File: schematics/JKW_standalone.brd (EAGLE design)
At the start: 159.4 x 80.7 mm, 221 parts, among them IC1 4093D, IC2 AT-MEGA-8, IC4 ATMEGA2560-16AU, T1 Mouser: 771-2N7002BK215 , N-C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, T10 Mouser: 771-2N7002BK215 , N-C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, T11 Mouser: 771-2N7002BK215 , N-C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, T12 Mouser: 771-2N7002BK215 , N-C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, T2 Mouser: 771-2N7002BK215 , N-C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, T3 Mouser: 771-2N7002BK215 , N-C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, T4 T-IRLMS6702, T5 Mouser: 771-2N7002BK215 , N-C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, T6 Mouser: 771-2N7002BK215 , N-C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, T7 Mouser: 771-2N7002BK215 , N-C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, T8 Mouser: 771-2N7002BK215 , N-C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, T9 Mouser: 771-2N7002BK215 , N-C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

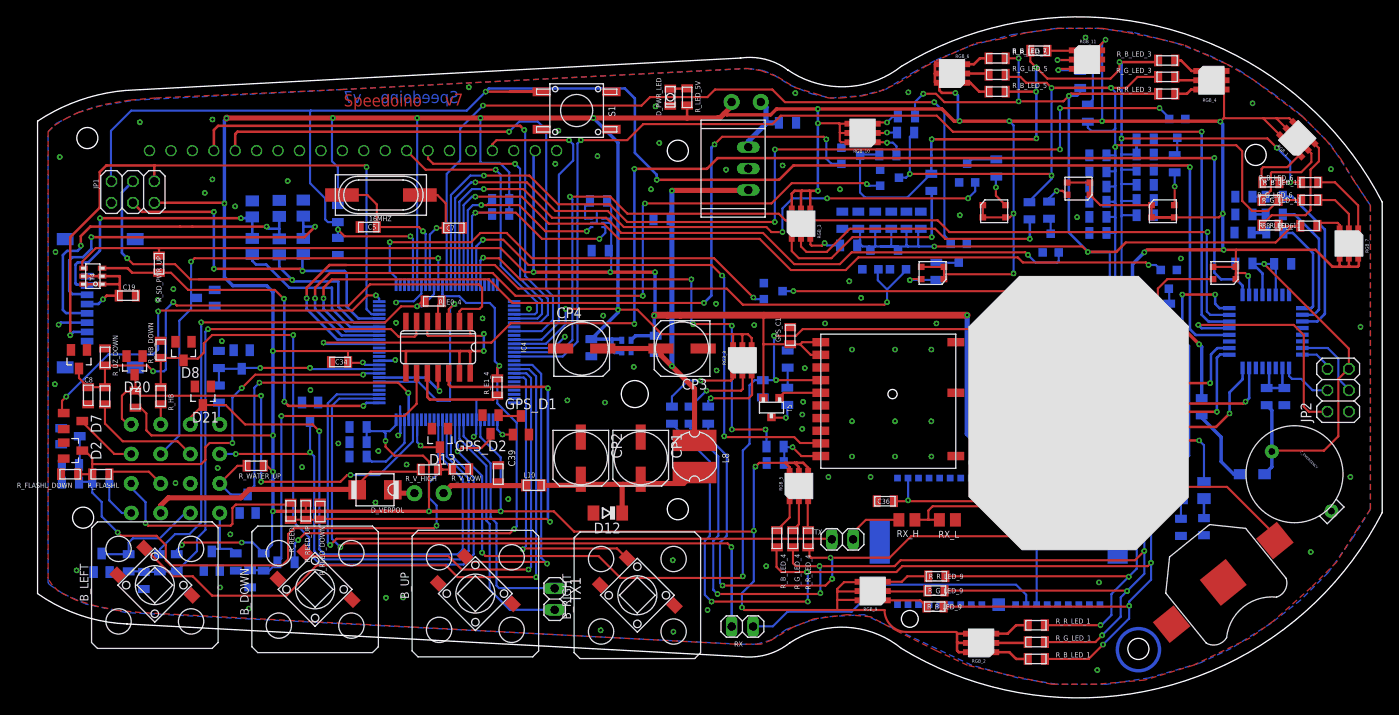
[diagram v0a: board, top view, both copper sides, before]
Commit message: Added Voltage measure wire, buffered
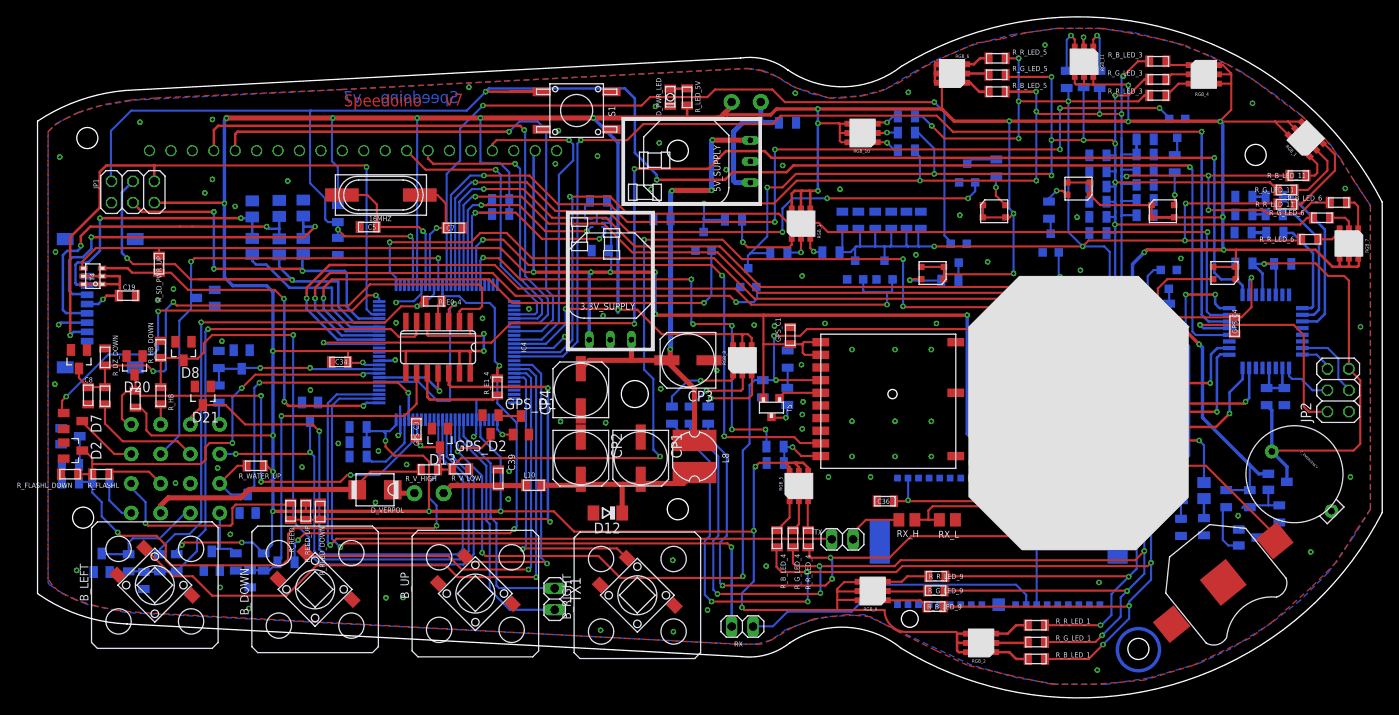
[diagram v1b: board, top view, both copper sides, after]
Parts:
- removed C4: 4.7µF, RCLDT:0805
- removed C6: 10uF, RCLDT:0805
- removed D11: Mouser 726-BAT60AE6327, diode:SOD323-W
- removed DC3.3: LXDC2HL33A-055, Kolja:LXDC2HL33A-055
- removed PWR_R78: R-7805-1.0, Kolja:SIP3
- removed R_L3: 0R, RCLDT:0805
- added 3.3V_SUPPLY: OKI78SR3.31.5WHC, Kolja:OKI-78SR
- added 5V_SUPPLY: OKI78SR51.5W36HC, Kolja:OKI-78SR
- added GPS_C3, GPS_C4: 100nF, RCLDT:0805
- added R_L4, R_L5: 2,1K, RCLDT:0805
- added R_L6: 21k, RCLDT:0805
- added T13: (no value), transistor:SOT23-BEC
- added U$14: 2N7002K, Kolja:SOT23
- IC2: value AT-MEGA-8 -> AT-MEGA-8L
- moved T11 30.4 mm to (117.6, 43.2)
- moved R_G_LED_2 30.1 mm to (87.9, 48.2), turned to 0 degrees
- moved R_B_LED_2 23.9 mm to (82.5, 52.0), turned to 0 degrees
- moved T2 20.5 mm to (84.2, 45.2), turned to 180 degrees
- moved T1 20.2 mm to (79.0, 49.5), turned to 180 degrees
- moved R_B_LED_7 7.96 mm to (125.9, 68.7), flipped to the bottom, turned to 270 degrees
- moved CP4 4.90 mm to (64.4, 31.9), turned to 90 degrees
- moved R_B_LED_6 4.16 mm to (154.2, 54.1)
- moved R_G_LED_7 4.13 mm to (124.0, 68.8)
- moved RGB_11 3.41 mm to (125.7, 69.3), turned to 90 degrees
- moved R_B_LED_11 3.30 mm to (149.4, 57.3), turned to 180 degrees
- moved R_R_LED_11 3.14 mm to (148.0, 53.9), turned to 180 degrees
- moved R_G_LED_6 2.52 mm to (152.2, 52.3)
- moved R_B_LED_8 2.26 mm to (103.0, 60.3), turned to 180 degrees
- moved R_R_LED_2 2.25 mm to (94.0, 48.2)
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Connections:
- removed net N$70: D11.A, R_L3.1
- new net N$86: R_L6.2, U$14.1
- new net N$87: R_L4.1, U$14.3
- new net N$88: R_L4.2, R_L5.2, T13.B
- net +3V3_EXT: now also 3.3V_SUPPLY.OUT; no longer C6.2, DC3.3.V_OUT
- net A2: now also GPS_C3.2, GPS_C4.2, IC2.2
- net BAT+: now also 3.3V_SUPPLY.IN, 5V_SUPPLY.IN; no longer PWR_R78.IN
- net GND: now also 3.3V_SUPPLY.GND, 5V_SUPPLY.GND, GPS_C3.1, GPS_C4.1, U$14.2; no longer C4.1, C6.1, DC3.3.GND, PWR_R78.GND
- net N$19: now also 5V_SUPPLY.OUT; no longer PWR_R78.OUT
- net VDD: now also R_L5.1, R_L6.1, T13.E; no longer C4.2, DC3.3.EN, DC3.3.V_IN, IC2.2, R_L3.2
- net V_AT8_BUFFERED: now also T13.C; no longer D11.C
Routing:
- net A2: track 12.0 -> 150.4 mm, vias 1 -> 6
- net GREEN_INSTR: track 277.0 -> 319.4 mm, vias 11 -> 16
- net BLUE_INSTR: track 292.3 -> 323.5 mm, vias 14 -> 17
- net D9: track 94.3 -> 63.5 mm, vias 4 -> 2
- net D13: track 53.4 -> 84.0 mm
- net N$71: track 37.5 -> 6.97 mm, vias 2 -> 0
- net N$55: track 32.6 -> 3.52 mm
- net D8: track 92.5 -> 67.5 mm, vias 4 -> 2
- net RED_INSTR: track 288.5 -> 305.5 mm, vias 12 -> 15
- net N$56: track 25.3 -> 9.86 mm
- net V_AT8_BUFFERED: track 53.3 -> 62.8 mm
- net N$70: track 9.31 -> 0.00 mm
- net BAT+: track 50.5 -> 59.7 mm, vias 2 -> 4
- net VDD: track 783.9 -> 792.3 mm, vias 41 -> 38
- net N$19: track 8.06 -> 16.2 mm
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
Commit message: Added PWR Pads, Added second 100nF cap to reduce ripple at the GPS, added resistors to save the z-diodes from over current
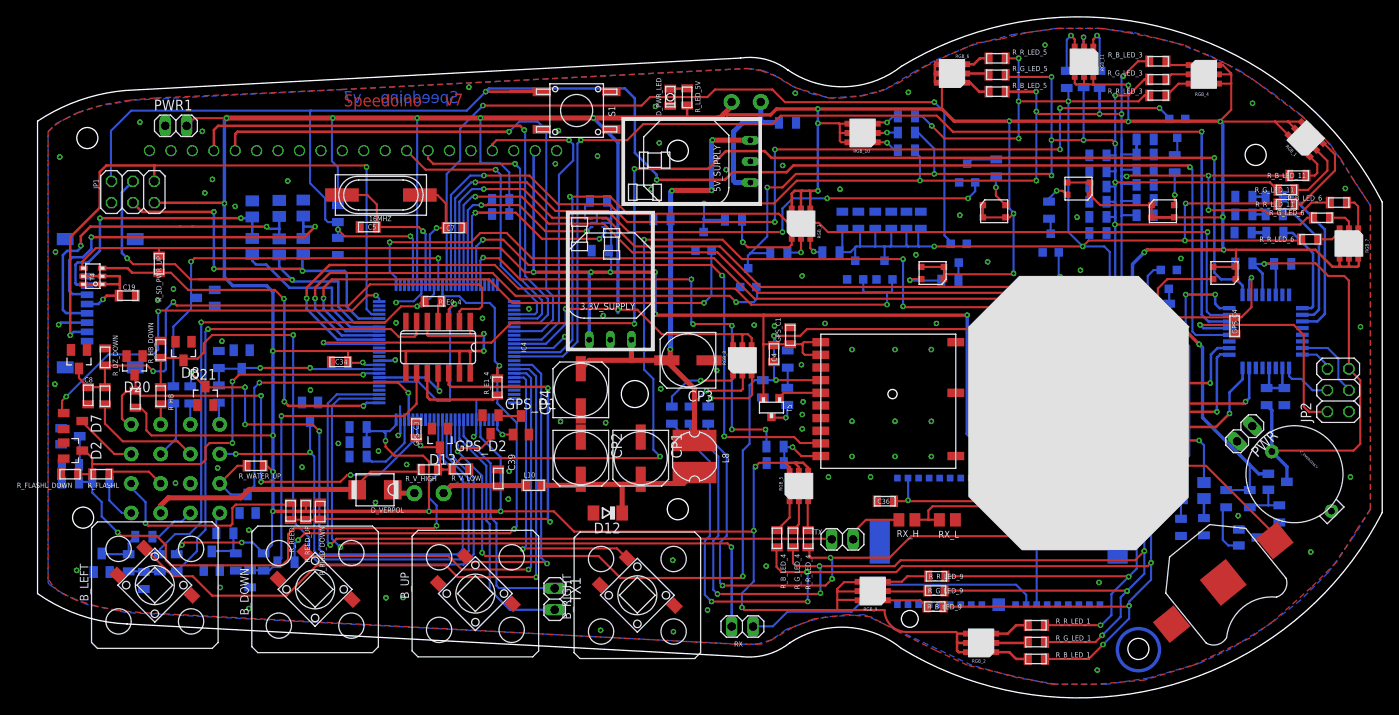
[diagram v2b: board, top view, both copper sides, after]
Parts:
- added C4: 100nF, RCLDT:0805
- added PWR, PWR1: (no value), pinhead:1X02
- added R_HB1, R_HB2, R_HB3, R_HB4: 600R, RCLDT:0805
- moved D21 0.30 mm to (19.9, 31.2), turned to 0 degrees
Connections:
- new net N$70: R_HB1.1, SPEEDOSTECKER.P$3
- new net N$89: R_HB2.1, SPEEDOSTECKER.P$14
- new net N$90: D18.3, R_E1_1.1, R_HB3.2
- new net N$92: R_HB4.1, SPEEDOSTECKER.P$7
- net +3V3_EXT: now also C4.2
- net D48: now also R_HB4.2; no longer SPEEDOSTECKER.P$7
- net GND: now also C4.1, PWR.1, PWR1.1
- net N$41: now also R_HB2.2; no longer SPEEDOSTECKER.P$14
- net N$42: now also R_HB3.1; no longer D18.3, R_E1_1.1
- net OIL_PR_IN: now also R_HB1.2; no longer SPEEDOSTECKER.P$3
- net VDD: now also PWR.2, PWR1.2
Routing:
- net D48: track 57.6 -> 49.0 mm
- net N$41: track 13.4 -> 5.64 mm
- net N$92: track 0.00 -> 6.85 mm
- net VDD: track 792.3 -> 798.3 mm
- net N$89: track 0.00 -> 5.64 mm
- net N$90: track 0.00 -> 5.09 mm
- net N$42: track 7.45 -> 2.57 mm
- net OIL_PR_IN: track 65.9 -> 70.1 mm, vias 1 -> 4
- net N$70: track 0.00 -> 2.48 mm
- net N$88: track 7.17 -> 5.43 mm
- net BL_L_IN: track 47.6 -> 48.8 mm

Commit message: BAT60A instead of TT
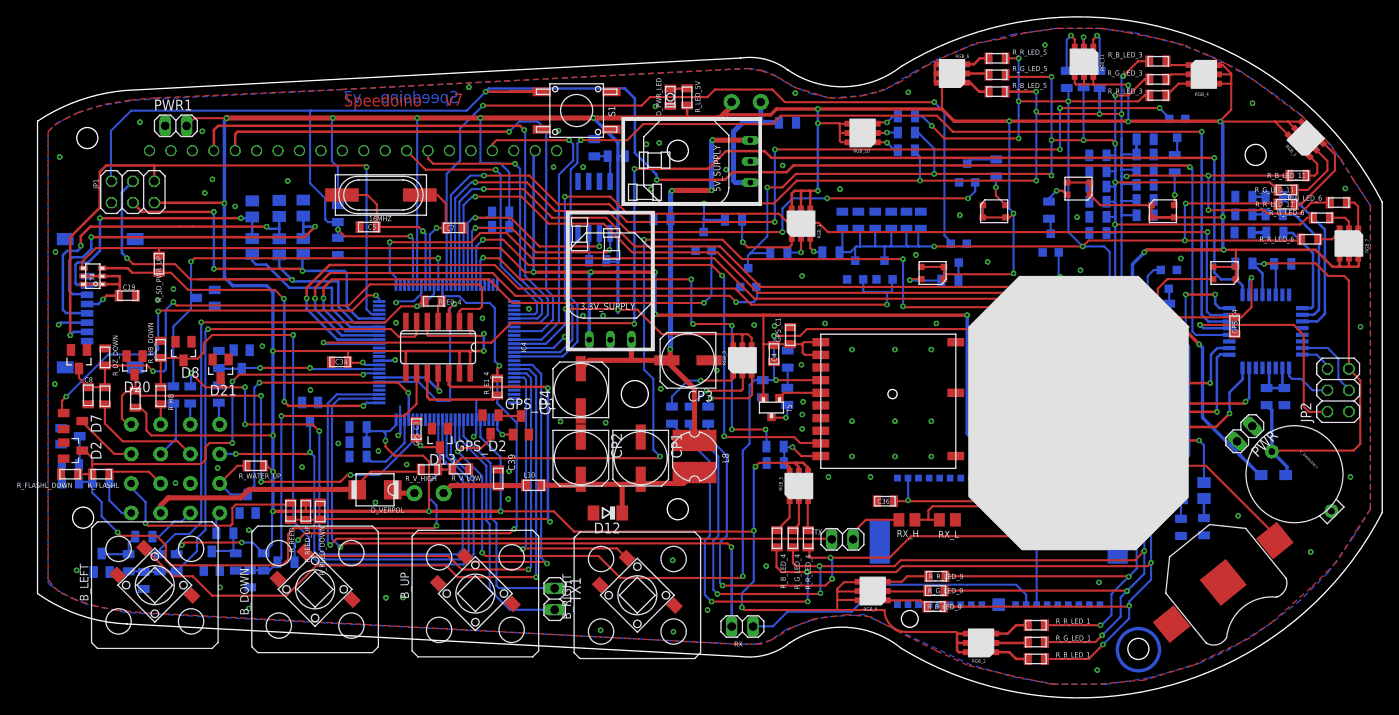
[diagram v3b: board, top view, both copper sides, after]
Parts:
- removed C9: 100nF, RCLDT:0805
- removed R_L4, R_L5: 2,1K, RCLDT:0805
- removed R_L6: 21k, RCLDT:0805
- removed R_TEMP_ALERT: 1k, RCLDT:0805
- removed T13: (no value), transistor:SOT23-BEC
- removed TMP102AIDRLT: TMP102, SparkFun:SOT563
- removed U$14: 2N7002K, Kolja:SOT23
- added C6: 10µF, RCLDT:0805
- added D9: Mouser 726-BAT60AE6327, diode:SOD323-W
- added R_DELAY: 300R, RCLDT:0805
- added R_TEMP_OS: 10K, RCLDT:0805
- added TEMP_SENS: SE95D, Kolja:SOIC8
- moved D21 3.67 mm to (21.7, 34.4), turned to 180 degrees
- moved R_SCL_UP 1.50 mm to (54.9, 52.9)
- moved R_SDA_UP 1.50 mm to (54.9, 51.2)
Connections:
- removed net N$86: R_L6.2, U$14.1
- removed net N$87: R_L4.1, U$14.3
- removed net N$88: R_L4.2, R_L5.2, T13.B
- new net N$91: R_TEMP_OS.1, TEMP_SENS.3
- net +3V3_EXT: no longer C9.1, R_TEMP_ALERT.2, TMP102AIDRLT.4, TMP102AIDRLT.5
- net GND: now also C6.2, TEMP_SENS.4, TEMP_SENS.5, TEMP_SENS.6, TEMP_SENS.7; no longer C9.2, TMP102AIDRLT.2, U$14.2
- net N$4: now also C6.1, R_DELAY.1, TEMP_SENS.8; no longer R_TEMP_ALERT.1, TMP102AIDRLT.3
- net SCL: now also TEMP_SENS.2; no longer TMP102AIDRLT.1
- net SDA: now also TEMP_SENS.1; no longer TMP102AIDRLT.6
- net VDD: now also D9.A, R_DELAY.2, R_TEMP_OS.2; no longer R_L5.1, R_L6.1, T13.E
- net V_AT8_BUFFERED: now also D9.C; no longer T13.C
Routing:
- net +3V3_EXT: track 219.0 -> 208.0 mm, vias 9 -> 8
- net N$86: track 6.22 -> 0.00 mm
- net N$88: track 5.43 -> 0.00 mm
- net N$87: track 3.97 -> 0.00 mm
- net N$91: track 0.00 -> 3.28 mm
- net VDD: track 798.3 -> 796.4 mm
- net GND: track 28.6 -> 26.8 mm, vias 96 -> 98
- net SCL: track 26.8 -> 28.4 mm
- net N$4: track 3.13 -> 4.71 mm
- net OIL_PR_IN: track 70.1 -> 71.2 mm
- net RX3: track 114.2 -> 115.1 mm
- net TX3: track 133.2 -> 133.8 mm
- net V_AT8_BUFFERED: track 62.8 -> 62.1 mm

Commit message: Added PortMultiplexer
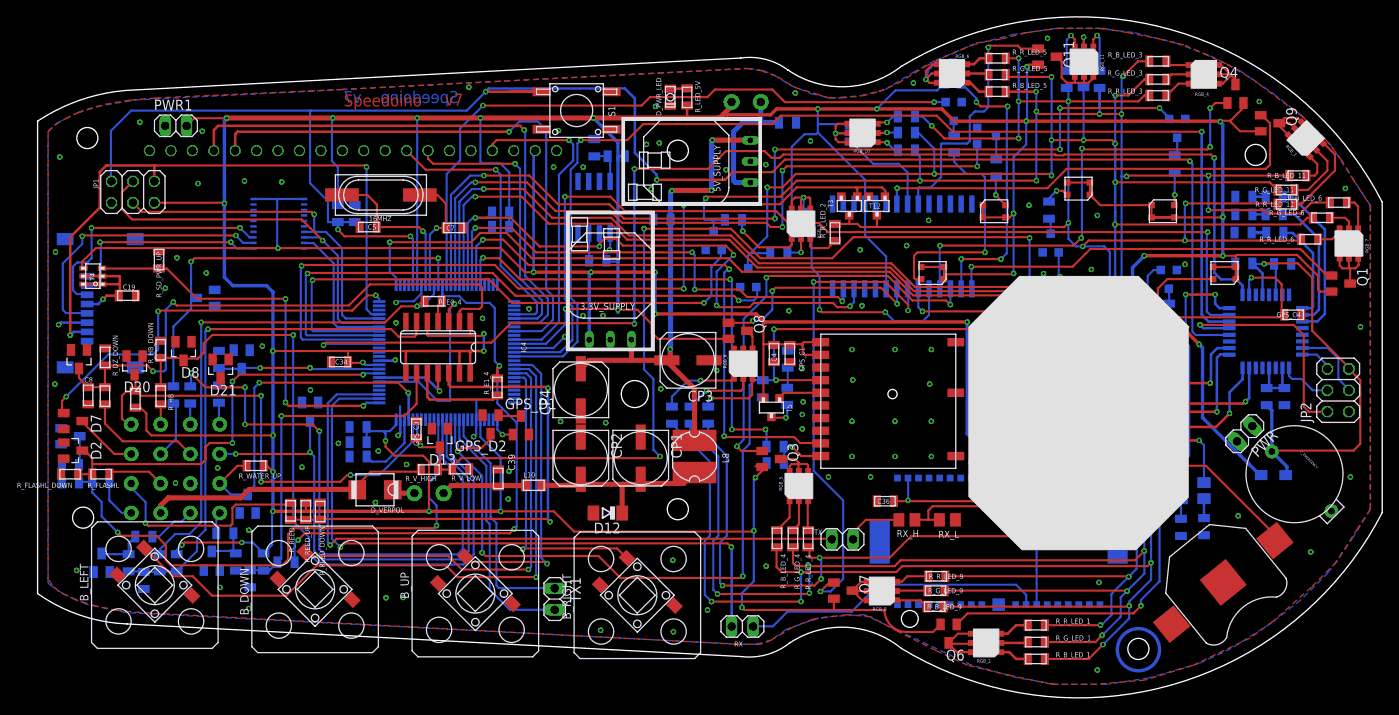
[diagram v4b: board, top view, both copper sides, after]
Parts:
- removed C10, C12, C13, C14, C15, C16, C17, C20, C21, C22, C23, C24, C25, C26, C27, C28, C29, C30: 100nF, RCLDT:0805
- removed R_CS_H, R_DI_H, R_SCK_H: 1k2, resistor:M0805
- removed R_CS_L, R_DI_L, R_SCK_L: 2k7, resistor:M0805
- added Q1, Q10, Q11, Q2, Q3, Q4, Q5, Q6, Q7, Q8, Q9: BSS84, transistor-small-signal:SOT23
- added U$14: 74LVC_LVCH245A, Kolja:TSSOP20
- added U$19: MCP23017, Kolja:SOIC28
- moved T8 16.8 mm to (108.6, 64.9)
- moved R_OIL 16.2 mm to (108.6, 61.0), turned to 90 degrees
- moved T12 7.65 mm to (99.5, 53.7), flipped to the top, turned to 0 degrees
- moved T3 7.63 mm to (96.2, 53.7), flipped to the top, turned to 0 degrees
- moved GPS_C4 7.02 mm to (148.8, 40.8), turned to 180 degrees
- moved T10 4.96 mm to (112.5, 62.0), turned to 270 degrees
- moved C35 4.38 mm to (37.6, 52.8), turned to 90 degrees
- moved R_R_LED_2 2.37 mm to (94.5, 50.5), flipped to the top, turned to 90 degrees
- moved GPS_C1 2.13 mm to (89.2, 36.2), turned to 90 degrees
- moved T1 1.20 mm to (80.2, 49.6)
- moved RGB_9 1.10 mm to (98.6, 6.40)
- moved RGB_2 0.60 mm to (111.0, 0.25)
- moved R_SD_PWR_UP 0.50 mm to (14.4, 47.3)
- moved RGB_8 0.41 mm to (82.0, 36.5)
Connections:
- new net N$100: Q3.1, U$19.3
- new net N$101: Q4.1, U$19.4
- new net N$102: Q5.1, U$19.5
- new net N$103: Q6.1, U$19.6
- new net N$104: Q7.1, U$19.7
- new net N$105: Q8.1, U$19.8
- new net N$106: Q9.1, U$19.21
- new net N$107: Q10.1, U$19.22
- new net N$108: Q11.1, U$19.23
- new net N$86: Q8.3, RGB_8.1+, RGB_8.2+, RGB_8.3+
- new net N$87: Q7.3, RGB_9.1+, RGB_9.2+, RGB_9.3+
- new net N$88: Q1.3, RGB_7.1+, RGB_7.2+, RGB_7.3+
- new net N$93: Q2.3, RGB_6.1+, RGB_6.2+, RGB_6.3+
- new net N$94: Q3.3, RGB_5.1+, RGB_5.2+, RGB_5.3+
- new net N$95: Q4.3, RGB_4.1+, RGB_4.2+, RGB_4.3+
- new net N$96: Q6.3, RGB_2.1+, RGB_2.2+, RGB_2.3+
- new net N$97: Q5.3, RGB_3.1+, RGB_3.2+, RGB_3.3+
- new net N$98: Q1.1, U$19.1
- new net N$99: Q2.1, U$19.2
- new net SD_CD: ST2.2, U$14.11
- new net SD_CLK: ST2.5, U$14.12
- new net SD_DATA_IN: ST2.3, U$14.13
- net +3V3_EXT: now also U$14.1, U$14.20
- net BLUE_INSTR: no longer C12.2, C13.2, C14.2, C15.2, C16.2, C17.2
- net D51: now also U$14.7; no longer R_CS_H.2
- net D52: now also U$14.8; no longer R_SCK_H.2
- net D53: now also U$14.9; no longer R_DI_H.2
- net GND: now also U$14.10, U$14.19, U$19.10, U$19.15, U$19.16, U$19.17; no longer C10.1, C12.1, C13.1, C14.1, C15.1, C16.1, C17.1, C20.1, C21.1, C22.1, C23.1, C24.1, C25.1, C26.1, C27.1, C28.1, C29.1, C30.1, R_CS_L.1, R_DI_L.1, R_SCK_L.1
- net GREEN_INSTR: no longer C10.2, C20.2, C21.2, C22.2, C23.2, C24.2
- net N$13: now also Q11.3, RGB_11.1+, RGB_11.2+, RGB_11.3+; no longer R_CS_H.1, R_CS_L.2, ST2.3
- net N$23: now also Q10.3, RGB_10.1+, RGB_10.2+, RGB_10.3+; no longer R_SCK_H.1, R_SCK_L.2, ST2.5
- net N$26: now also Q9.3, RGB_1.1+, RGB_1.2+, RGB_1.3+; no longer R_DI_H.1, R_DI_L.2, ST2.2
- net RED_INSTR: no longer C25.2, C26.2, C27.2, C28.2, C29.2, C30.2
- net SCL: now also U$19.12
- net SDA: now also U$19.13
- net VDD: now also Q1.2, Q10.2, Q11.2, Q2.2, Q3.2, Q4.2, Q5.2, Q6.2, Q7.2, Q8.2, Q9.2, U$19.18, U$19.9; no longer RGB_1.1+, RGB_1.2+, RGB_1.3+, RGB_10.1+, RGB_10.2+, RGB_10.3+, RGB_11.1+, RGB_11.2+, RGB_11.3+, RGB_2.1+, RGB_2.2+, RGB_2.3+, RGB_3.1+, RGB_3.2+, RGB_3.3+, RGB_4.1+, RGB_4.2+, RGB_4.3+, RGB_5.1+, RGB_5.2+, RGB_5.3+, RGB_6.1+, RGB_6.2+, RGB_6.3+, RGB_7.1+, RGB_7.2+, RGB_7.3+, RGB_8.1+, RGB_8.2+, RGB_8.3+, RGB_9.1+, RGB_9.2+, RGB_9.3+
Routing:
- net N$103: track 0.00 -> 85.6 mm, vias 0 -> 5
- net N$104: track 0.00 -> 57.7 mm, vias 0 -> 3
- net N$101: track 0.00 -> 55.1 mm, vias 0 -> 5
- net N$106: track 0.00 -> 53.6 mm, vias 0 -> 1
- net N$100: track 0.00 -> 50.0 mm, vias 0 -> 3
- net N$98: track 0.00 -> 47.5 mm, vias 0 -> 1
- net VDD: track 796.4 -> 749.9 mm, vias 38 -> 36
- net SCL: track 28.4 -> 71.2 mm, vias 2 -> 5
- net SDA: track 28.2 -> 62.4 mm, vias 2 -> 5
- net N$99: track 0.00 -> 33.6 mm, vias 0 -> 4
- net SD_CLK: track 0.00 -> 33.4 mm, vias 0 -> 2
- net N$13: track 41.6 -> 9.65 mm, vias 2 -> 0
- net N$108: track 0.00 -> 31.4 mm, vias 0 -> 1
- net SD_DATA_IN: track 0.00 -> 30.6 mm, vias 0 -> 2
- net N$23: track 40.2 -> 11.0 mm, vias 2 -> 1
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
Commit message: Improved schematic
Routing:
- net RED_INSTR: track 287.7 -> 287.1 mm
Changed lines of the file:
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@@
 <?xml version="1.0" encoding="utf-8"?>
 <!DOCTYPE eagle SYSTEM "eagle.dtd">
-<eagle version="6.1">
+<eagle version="6.2">
 <drawing>
 <settings>
@@
 <contactref element="D_P_MCCOI" pad="1"/>
 <via x="86.325" y="58.6" extent="1-16" drill="0.3"/>
-<via x="105.625" y="52" extent="1-16" drill="0.3"/>
+<via x="105.625" y="52.2" extent="1-16" drill="0.3"/>
 <via x="97.725" y="41.875" extent="1-16" drill="0.3"/>
 <via x="103.825" y="68.275" extent="1-16" drill="0.3"/>
@@
 <wire x1="146.884" y1="54" x2="146.984" y2="53.9" width="0.254" layer="1"/>
 <wire x1="94.525" y1="51.566" x2="96.2" y2="51.566" width="0.254" layer="1"/>
-<wire x1="96.2" y1="51.566" x2="97.2021" y2="51.566" width="0.254" layer="1"/>
-<wire x1="97.2021" y1="51.566" x2="97.5681" y2="51.2" width="0.254" layer="1"/>
-<wire x1="97.5681" y1="51.2" x2="99.5" y2="51.2" width="0.254" layer="1"/>
-<wire x1="99.5" y1="51.2" x2="121.7" y2="51.2" width="0.254" layer="1"/>
-<wire x1="121.7" y1="51.2" x2="122.2" y2="51.7" width="0.254" layer="1"/>
 <via x="122.2" y="51.7" extent="1-16" drill="0.3"/>
 <wire x1="96.225" y1="52.5889" x2="96.225" y2="51.591" width="0.254" layer="1"/>
 <wire x1="96.225" y1="51.591" x2="96.2" y2="51.566" width="0.254" layer="1"/>
-<wire x1="99.5" y1="52.5889" x2="99.5" y2="51.2" width="0.254" layer="1"/>
 <wire x1="122.2" y1="49.8" x2="123.1" y2="48.9" width="0.254" layer="16"/>
 <wire x1="123.1" y1="48.9" x2="123.9" y2="48.9" width="0.254" layer="16"/>
+<wire x1="96.2" y1="51.566" x2="99.3" y2="51.566" width="0.254" layer="1"/>
+<wire x1="99.3" y1="51.566" x2="122.066" y2="51.566" width="0.254" layer="1"/>
+<wire x1="122.066" y1="51.566" x2="122.2" y2="51.7" width="0.254" layer="1"/>
+<wire x1="99.5" y1="52.5889" x2="99.5" y2="51.766" width="0.254" layer="1"/>
+<wire x1="99.5" y1="51.766" x2="99.3" y2="51.566" width="0.254" layer="1"/>
 </signal>
 <signal name="N$70">
